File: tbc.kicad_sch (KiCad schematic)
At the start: 0 parts

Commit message: initial work on schematic symbol creation
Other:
- added sheet Microcontroller, UI and Power (micro_ui.kicad_sch)
- added sheet Video Processing (video_proc.kicad_sch)
- company: (none) -> Wavelet Engineering Pty Ltd
- title: (none) -> Time Base Corrector
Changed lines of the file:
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@@
 (kicad_sch (version 20230121) (generator eeschema)
   (paper "A4")
+  (title_block
+    (title "Time Base Corrector")
+    (date "2024-01-15")
+    (rev "1")
+    (company "Wavelet Engineering Pty Ltd")
+  )
+  (sheet (at 149.86 80.01) (size 34.29 21.59) (fields_autoplaced)
+    (stroke (width 0.1524) (type solid))
+    (fill (color 0 0 0 0.0000))
+    (property "Sheetname" "Video Processing" (at 149.86 79.2984 0)
+      (effects (font (size 1.27 1.27)) (justify left bottom))
+    )
+    (property "Sheetfile" "video_proc.kicad_sch" (at 149.86 102.1846 0)
+      (effects (font (size 1.27 1.27)) (justify left top))
+    )
+    (instances
+      (project "tbc"
+        (path "/9df71e53-7941-4fd3-a17d-93619e4e3e02" (page "3"))
+      )
+    )
+  )
+  (sheet (at 110.49 80.01) (size 34.29 21.59) (fields_autoplaced)
+    (stroke (width 0.1524) (type solid))
+    (fill (color 0 0 0 0.0000))
+    (property "Sheetname" "Microcontroller, UI and Power" (at 110.49 79.2984 0)
+      (effects (font (size 1.27 1.27)) (justify left bottom))
+    )
+    (property "Sheetfile" "micro_ui.kicad_sch" (at 110.49 102.1846 0)
+      (effects (font (size 1.27 1.27)) (justify left top))
+    )
+    (instances
+      (project "tbc"
+        (path "/9df71e53-7941-4fd3-a17d-93619e4e3e02" (page "2"))
+      )
+    )
+  )
   (sheet_instances
     (path "/" (page "1"))

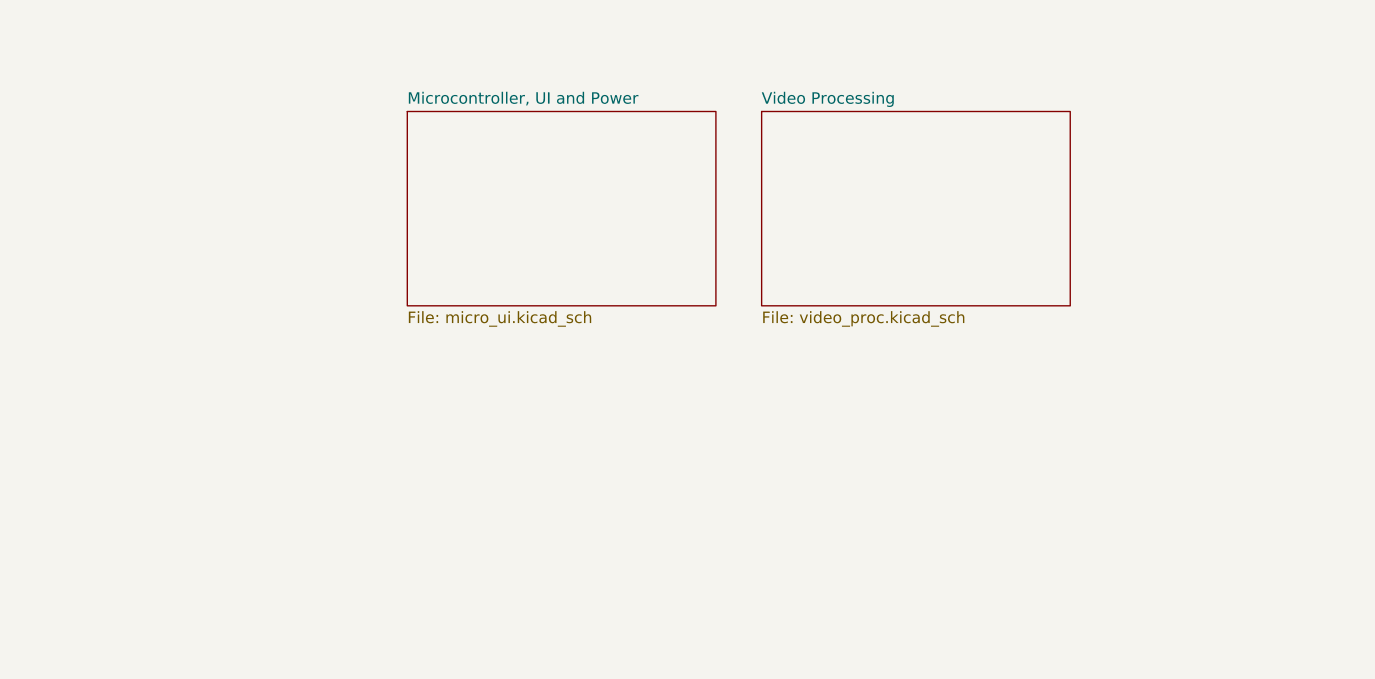
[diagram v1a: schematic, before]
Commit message: changed hierarchy, added symbols
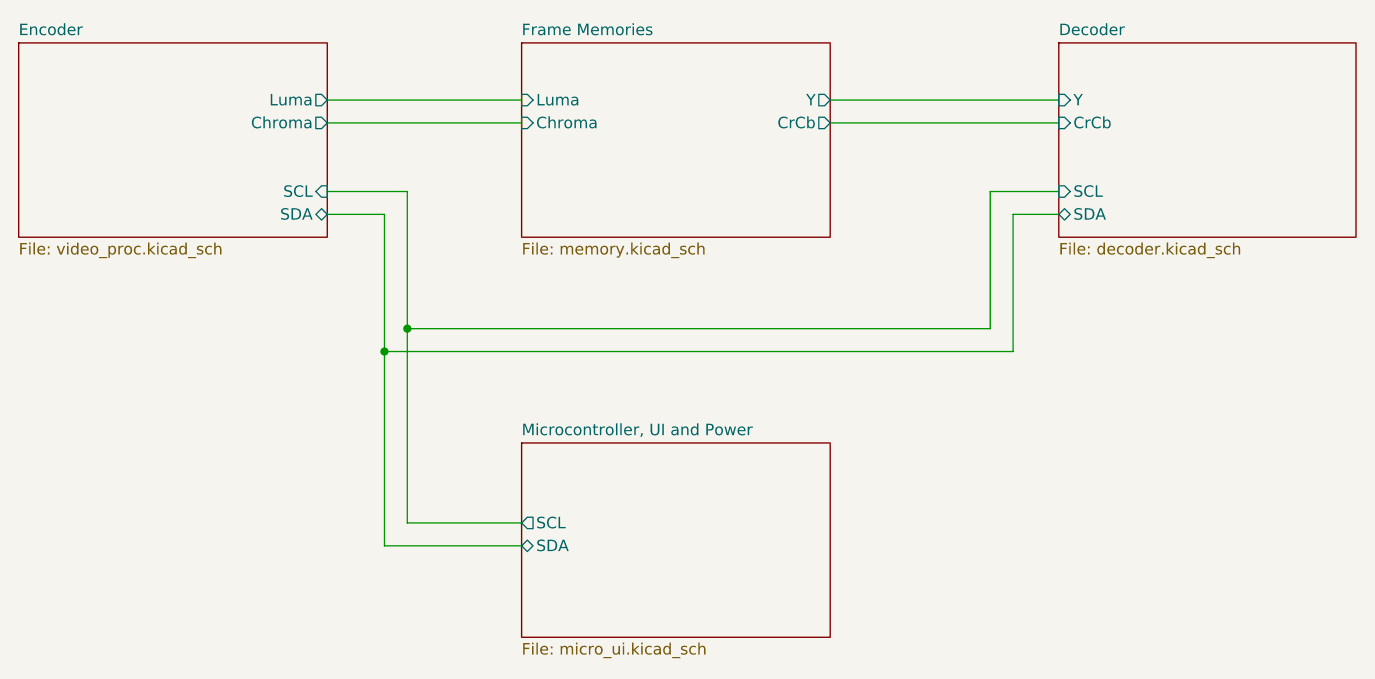
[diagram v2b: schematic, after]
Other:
- sheet Video Processing renamed Encoder
- added sheet Decoder (decoder.kicad_sch)
- added sheet Frame Memories (memory.kicad_sch)
- sheet Encoder ports: added Chroma, Luma, SCL, SDA; removed none
- sheet Microcontroller, UI and Power ports: added SCL, SDA; removed none
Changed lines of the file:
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@@
     (company "Wavelet Engineering Pty Ltd")
   )
-  (sheet (at 149.86 80.01) (size 34.29 21.59) (fields_autoplaced)
+  (junction (at 110.49 104.14) (diameter 0) (color 0 0 0 0)
+  )
+  (junction (at 107.95 106.68) (diameter 0) (color 0 0 0 0)
+  )
+  (wire (pts (xy 107.95 106.68) (xy 107.95 128.27))
+    (stroke (width 0) (type default))
+  )
+  (wire (pts (xy 175.26 88.9) (xy 175.26 104.14))
+    (stroke (width 0) (type default))
+  )
+  (wire (pts (xy 110.49 104.14) (xy 110.49 125.73))
+    (stroke (width 0) (type default))
+  )
+  (wire (pts (xy 107.95 128.27) (xy 123.19 128.27))
+    (stroke (width 0) (type default))
+  )
+  (wire (pts (xy 175.26 104.14) (xy 110.49 104.14))
+    (stroke (width 0) (type default))
+  )
+  (wire (pts (xy 107.95 91.44) (xy 107.95 106.68))
+    (stroke (width 0) (type default))
+  )
+  (wire (pts (xy 157.48 78.74) (xy 182.88 78.74))
+    (stroke (width 0) (type default))
+  )
+  (wire (pts (xy 101.6 78.74) (xy 123.19 78.74))
+    (stroke (width 0) (type default))
+  )
+  (wire (pts (xy 110.49 88.9) (xy 110.49 104.14))
+    (stroke (width 0) (type default))
+  )
+  (wire (pts (xy 177.8 106.68) (xy 107.95 106.68))
+    (stroke (width 0) (type default))
+  )
+  (wire (pts (xy 101.6 88.9) (xy 110.49 88.9))
+    (stroke (width 0) (type default))
+  )
+  (wire (pts (xy 182.88 88.9) (xy 175.26 88.9))
+    (stroke (width 0) (type default))
+  )
+  (wire (pts (xy 110.49 125.73) (xy 123.19 125.73))
+    (stroke (width 0) (type default))
+  )
+  (wire (pts (xy 182.88 91.44) (xy 177.8 91.44))
+    (stroke (width 0) (type default))
+  )
+  (wire (pts (xy 101.6 81.28) (xy 123.19 81.28))
+    (stroke (width 0) (type default))
+  )
+  (wire (pts (xy 101.6 91.44) (xy 107.95 91.44))
+    (stroke (width 0) (type default))
+  )
+  (wire (pts (xy 157.48 81.28) (xy 182.88 81.28))
+    (stroke (width 0) (type default))
+  )
+  (wire (pts (xy 177.8 91.44) (xy 177.8 106.68))
+    (stroke (width 0) (type default))
+  )
+  (sheet (at 67.31 72.39) (size 34.29 21.59) (fields_autoplaced)
     (stroke (width 0.1524) (type solid))
     (fill (color 0 0 0 0.0000))
-    (property "Sheetname" "Video Processing" (at 149.86 79.2984 0)
+    (property "Sheetname" "Encoder" (at 67.31 71.6784 0)
       (effects (font (size 1.27 1.27)) (justify left bottom))
     )
-    (property "Sheetfile" "video_proc.kicad_sch" (at 149.86 102.1846 0)
+    (property "Sheetfile" "video_proc.kicad_sch" (at 67.31 94.5646 0)
       (effects (font (size 1.27 1.27)) (justify left top))
+    )
+    (pin "SCL" input (at 101.6 88.9 0)
+      (effects (font (size 1.27 1.27)) (justify right))
+    )
+    (pin "SDA" bidirectional (at 101.6 91.44 0)
+      (effects (font (size 1.27 1.27)) (justify right))
+    )
+    (pin "Chroma" output (at 101.6 81.28 0)
+      (effects (font (size 1.27 1.27)) (justify right))
+    )
+    (pin "Luma" output (at 101.6 78.74 0)
+      (effects (font (size 1.27 1.27)) (justify right))
+    )
+    (instances
+      (project "tbc"
+        (path "/9df71e53-7941-4fd3-a17d-93619e4e3e02" (page "2"))
+      )
+    )
+  )
+  (sheet (at 123.19 116.84) (size 34.29 21.59) (fields_autoplaced)
+    (stroke (width 0.1524) (type solid))
+    (fill (color 0 0 0 0.0000))
+    (property "Sheetname" "Microcontroller, UI and Power" (at 123.19 116.1284 0)
+      (effects (font (size 1.27 1.27)) (justify left bottom))
+    )
+    (property "Sheetfile" "micro_ui.kicad_sch" (at 123.19 139.0146 0)
+      (effects (font (size 1.27 1.27)) (justify left top))
+    )
+    (pin "SDA" bidirectional (at 123.19 128.27 180)
+      (effects (font (size 1.27 1.27)) (justify left))
+    )
+    (pin "SCL" output (at 123.19 125.73 180)
+      (effects (font (size 1.27 1.27)) (justify left))
     )
     (instances
@@
     )
   )
-  (sheet (at 110.49 80.01) (size 34.29 21.59) (fields_autoplaced)
+  (sheet (at 123.19 72.39) (size 34.29 21.59) (fields_autoplaced)
     (stroke (width 0.1524) (type solid))
     (fill (color 0 0 0 0.0000))
-    (property "Sheetname" "Microcontroller, UI and Power" (at 110.49 79.2984 0)
+    (property "Sheetname" "Frame Memories" (at 123.19 71.6784 0)
       (effects (font (size 1.27 1.27)) (justify left bottom))
     )
-    (property "Sheetfile" "micro_ui.kicad_sch" (at 110.49 102.1846 0)
+    (property "Sheetfile" "memory.kicad_sch" (at 123.19 94.5646 0)
       (effects (font (size 1.27 1.27)) (justify left top))
+    )
+    (pin "Y" output (at 157.48 78.74 0)
+      (effects (font (size 1.27 1.27)) (justify right))
+    )
+    (pin "Luma" input (at 123.19 78.74 180)
+      (effects (font (size 1.27 1.27)) (justify left))
+    )
+    (pin "Chroma" input (at 123.19 81.28 180)
+      (effects (font (size 1.27 1.27)) (justify left))
+    )
+    (pin "CrCb" output (at 157.48 81.28 0)
+      (effects (font (size 1.27 1.27)) (justify right))
     )
     (instances
       (project "tbc"
-        (path "/9df71e53-7941-4fd3-a17d-93619e4e3e02" (page "2"))
+        (path "/9df71e53-7941-4fd3-a17d-93619e4e3e02" (page "4"))
       )
     )
+  )
+  (sheet (at 182.88 72.39) (size 33.02 21.59) (fields_autoplaced)
+    (stroke (width 0.1524) (type solid))
+    (fill (color 0 0 0 0.0000))
+    (property "Sheetname" "Decoder" (at 182.88 71.6784 0)
+      (effects (font (size 1.27 1.27)) (justify left bottom))
+    )
+    (property "Sheetfile" "decoder.kicad_sch" (at 182.88 94.5646 0)
+      (effects (font (size 1.27 1.27)) (justify left top))
+    )
+    (pin "SDA" bidirectional (at 182.88 91.44 180)
+      (effects (font (size 1.27 1.27)) (justify left))
+    )
+    (pin "SCL" input (at 182.88 88.9 180)
+      (effects (font (size 1.27 1.27)) (justify left))
+    )
+    (pin "Y" input (at 182.88 78.74 180)
+      (effects (font (size 1.27 1.27)) (justify left))
+    )
+    (pin "CrCb" input (at 182.88 81.28 180)
+      (effects (font (size 1.27 1.27)) (justify left))
+    )
+    (instances
+      (project "tbc"
+        (path "/9df71e53-7941-4fd3-a17d-93619e4e3e02" (page "5"))
+      )
+    )

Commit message: continuing schematic capture, renamed sheets
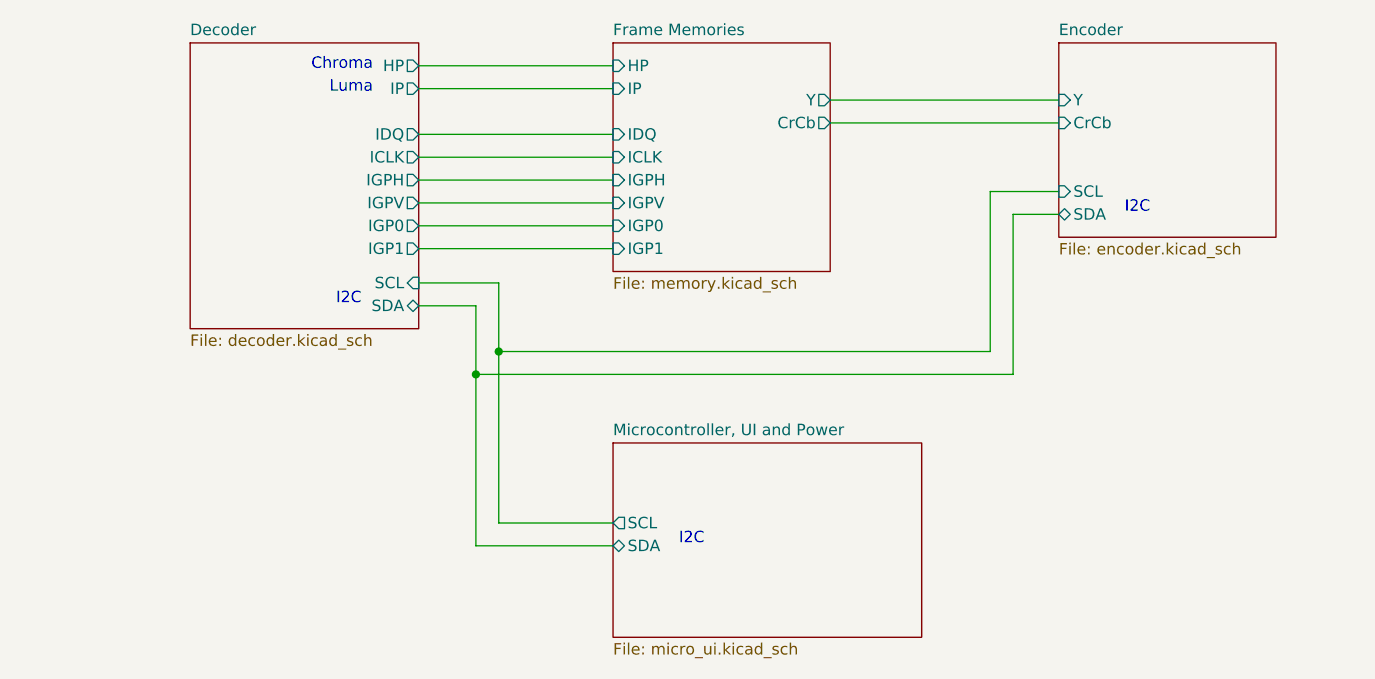
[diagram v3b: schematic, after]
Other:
- sheet Decoder ports: added HP, ICLK, IDQ, IGP0, IGP1, IGPH, IGPV, IP; removed CrCb, Y
- sheet Encoder: file video_proc.kicad_sch -> encoder.kicad_sch
- sheet Encoder ports: added CrCb, Y; removed Chroma, Luma
- sheet Frame Memories ports: added HP, ICLK, IDQ, IGP0, IGP1, IGPH, IGPV, IP; removed Chroma, Luma
- note added: "Chroma"
- note added: "I2C"
- note added: "Luma"

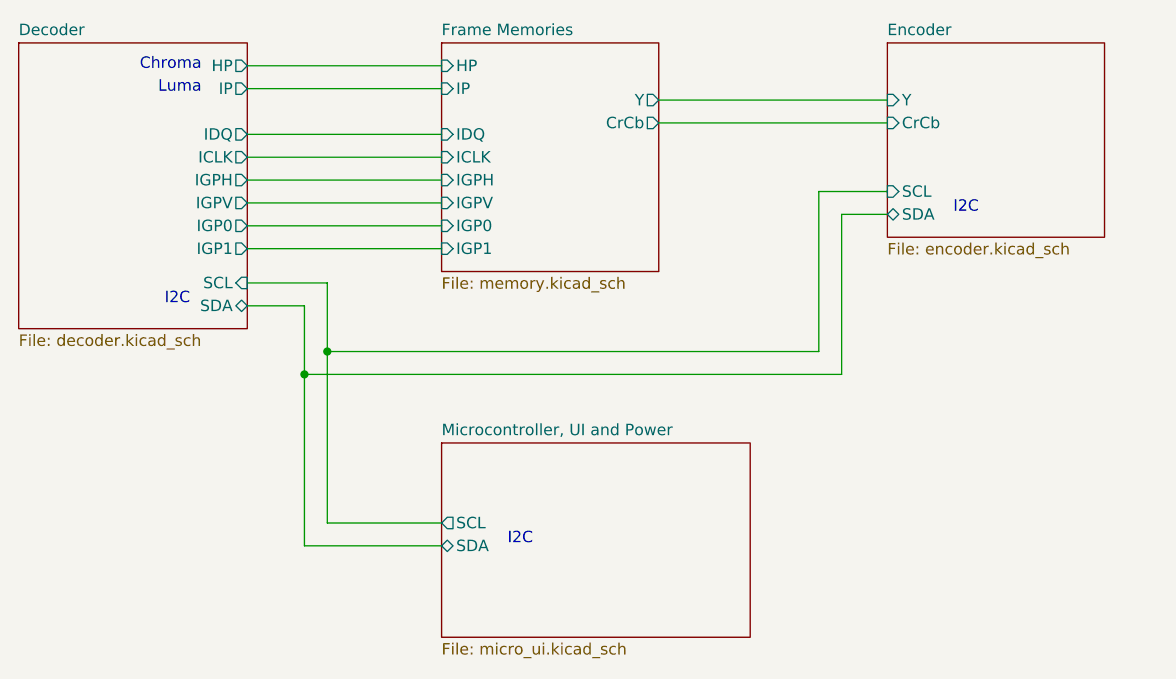
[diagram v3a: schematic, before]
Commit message: added decoder symbol
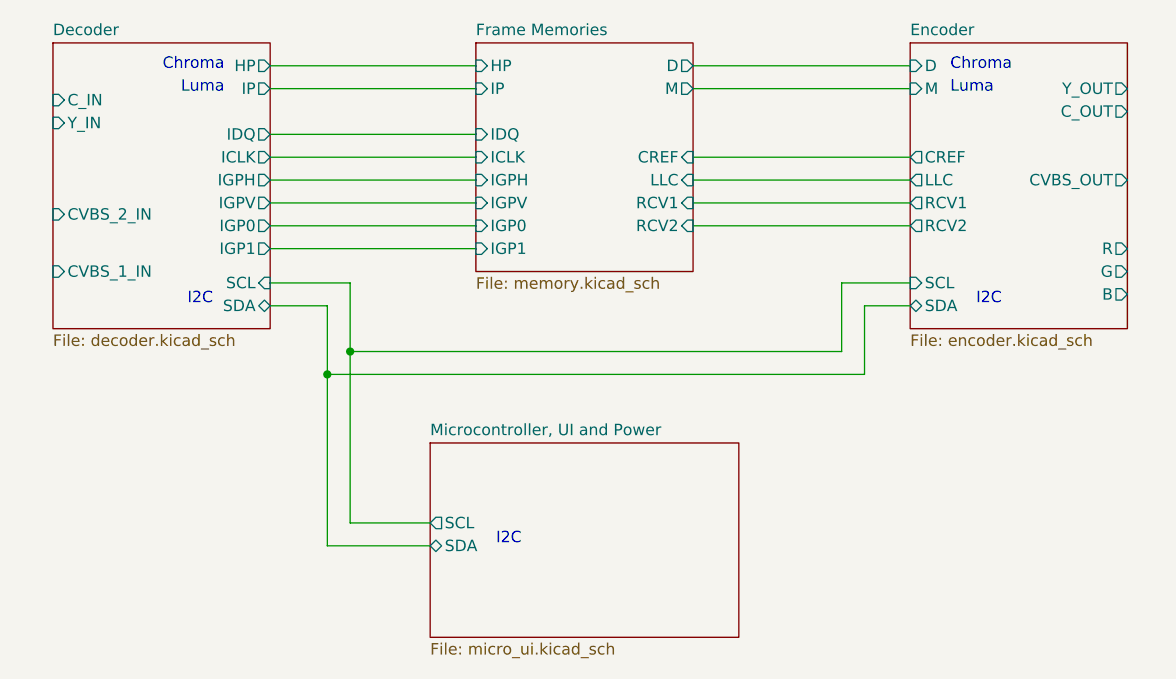
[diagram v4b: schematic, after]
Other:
- sheet Decoder ports: added CVBS_1_IN, CVBS_2_IN, C_IN, Y_IN; removed none
- sheet Encoder ports: added B, CREF, CVBS_OUT, C_OUT, D, G, LLC, M, R, RCV1, RCV2, Y_OUT; removed CrCb, Y
- sheet Frame Memories ports: added CREF, D, LLC, M, RCV1, RCV2; removed CrCb, Y

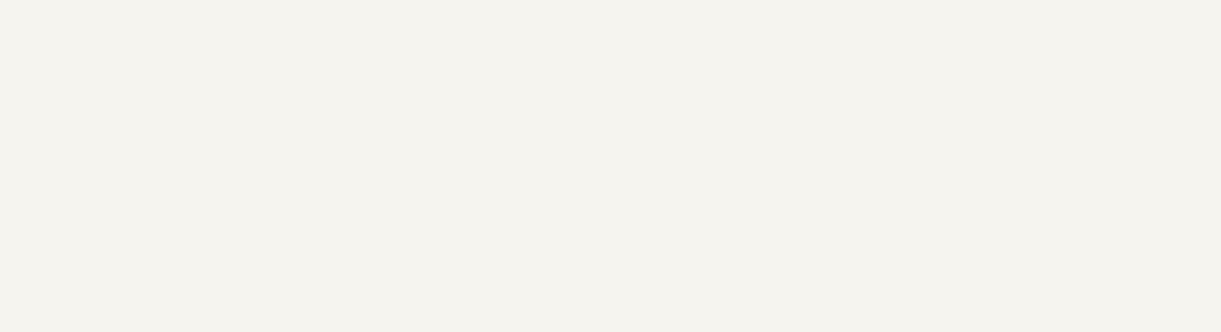
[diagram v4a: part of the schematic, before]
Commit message: added buses, title block info
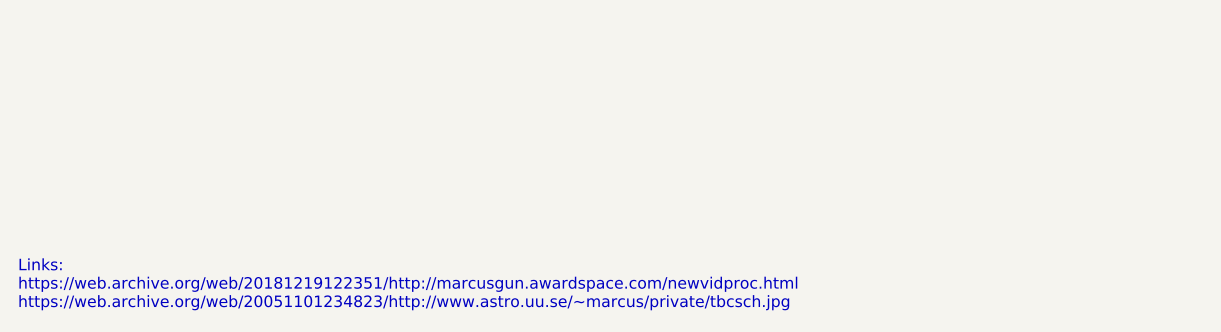
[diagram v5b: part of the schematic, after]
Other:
- note added: "Links: https://web.archive.org/web/20181219122351/http://marcusgun.awardspace.com/newvidproc.html https://web.archive.org/web/20051101234823/http://www.astro.uu.se/~marcus/private/tbcsch.jpg"
- company: Wavelet Engineering Pty Ltd -> Wavelet Engineering Pty Ltd (ACN 159 717 665)
- title: Time Base Corrector -> Time Base Corrector and Video Scaler
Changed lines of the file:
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@@
   (paper "A4")
   (title_block
-    (title "Time Base Corrector")
+    (title "Time Base Corrector and Video Scaler")
     (date "2024-01-15")
     (rev "1")
-    (company "Wavelet Engineering Pty Ltd")
+    (company "Wavelet Engineering Pty Ltd (ACN 159 717 665)")
+    (comment 1 "https://github.com/philmcm/tbc")
+    (comment 2 "Enhancements by Phil McMillan © 2024")
+    (comment 3 "(refer links on left)")
+    (comment 4 "Original TBC circuit design © 2001 Marcus Gunnarsson")
   )
   (junction (at 123.19 106.68) (diameter 0) (color 0 0 0 0)
@@
     (effects (font (size 1.27 1.27)) (justify left bottom))
   )
+  (text "Links:\nhttps://web.archive.org/web/20181219122351/http://marcusgun.awardspace.com/newvidproc.html\nhttps://web.archive.org/web/20051101234823/http://www.astro.uu.se/~marcus/private/tbcsch.jpg"
+    (at 16.51 194.31 0)
+    (effects (font (size 1.27 1.27)) (justify left bottom))
+  )
